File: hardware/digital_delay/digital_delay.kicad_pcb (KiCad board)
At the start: 2 copper layers, 50 parts, among them J2 Conn_01x04, J3 Conn_01x40, J4 Conn_01x02, J5 Conn_02x10_Top_Bottom, J6 Conn_02x10_Top_Bottom, U1 STM32H750XBHx, U2 PCM3060, U3 TPS63061, U4 TLV702475_SOT23-5, U5 AZ1117-3.3, Y1 Crystal, Y2 Crystal

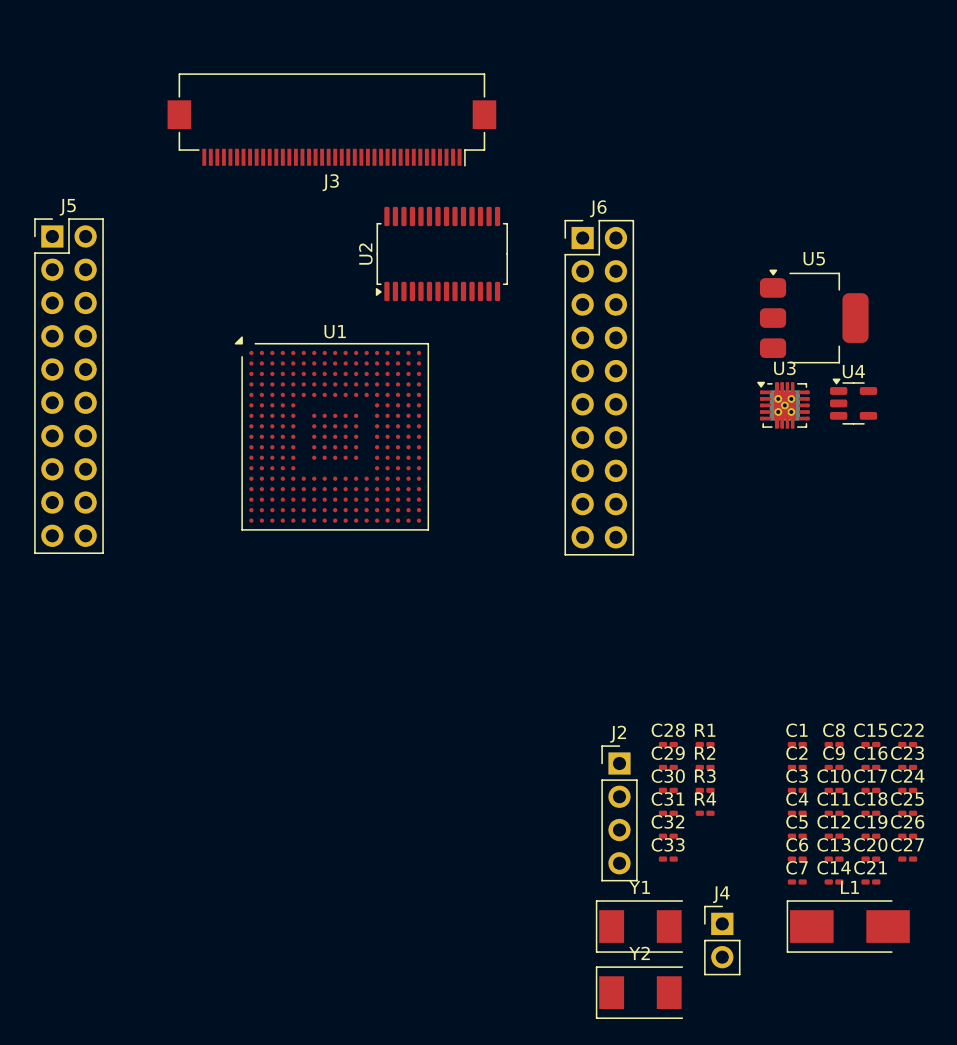
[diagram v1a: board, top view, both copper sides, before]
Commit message: basic design rules for 8 layer PCB
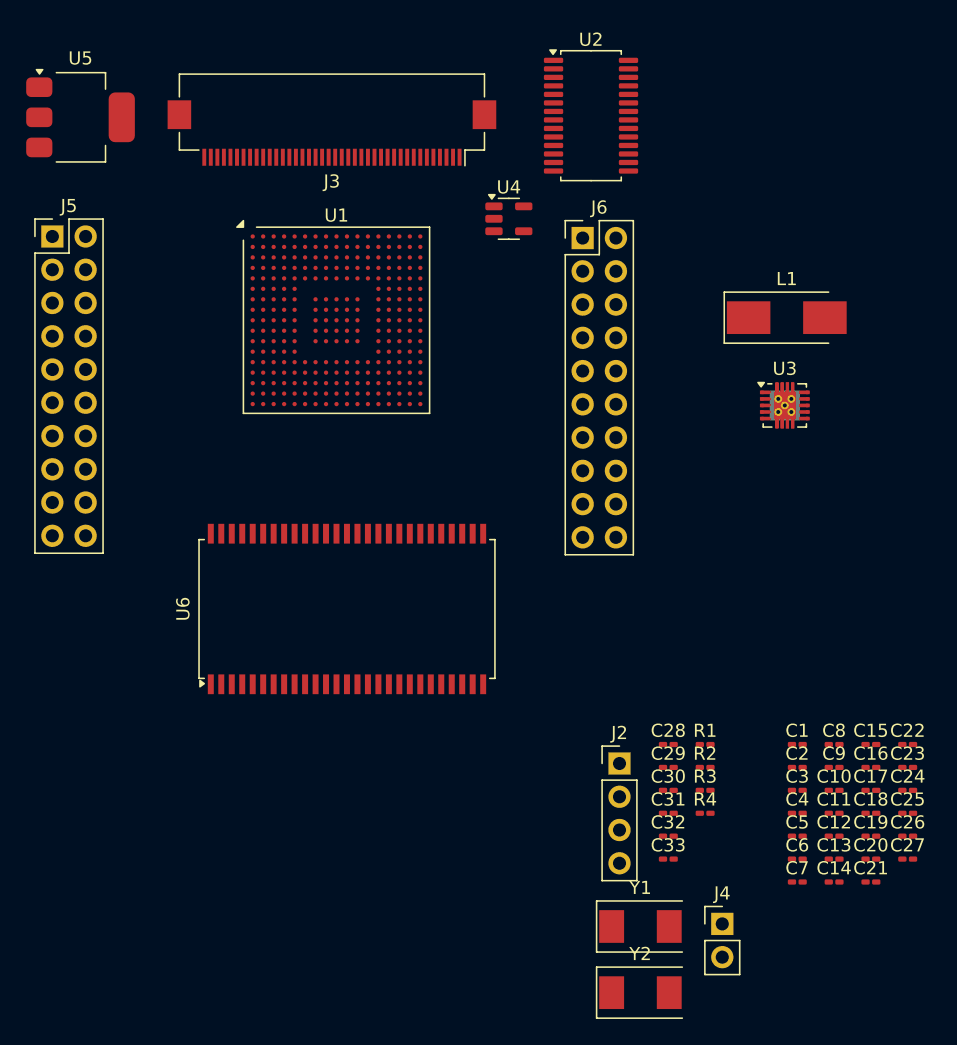
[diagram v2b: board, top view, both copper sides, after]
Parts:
- added U6: MT48LC16M16A2P, Package_SO:TSOP-II-54_22.2x10.16mm_P0.8mm, F.Cu at (99.0, 104.8)
- moved U5 58.1 mm to (78.7, 67.2)
- moved L1 46.7 mm to (132.6, 82.5)
- moved U4 29.9 mm to (111.4, 75.0)
- moved U2 15.5 mm to (117.6, 67.1), turned to 0 degrees
- moved U1 8.90 mm to (98.2, 82.7)
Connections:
- U1 pad A14: unconnected-(U1-PA15-PadA14) -> /JTAG_DI
- U1 pad B14: unconnected-(U1-PA14-PadB14) -> /JTAG_CLK
- U1 pad C15: unconnected-(U1-PA13-PadC15) -> /JTAG_MS
- U1 pad C6: unconnected-(U1-PB3-PadC6) -> /JTAG_DO
